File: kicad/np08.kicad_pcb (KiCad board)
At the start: 2 copper layers, 101.6 x 101.6 mm, 60 parts, among them P1 USB_B, P10 CONN_01X02, P11 CONN_01X02, P12 analog, P13 GND, P14 +5V, P15 CONN_01X08, P16 CONN_01X08, P2 CONN_01X04, P3 aliment.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

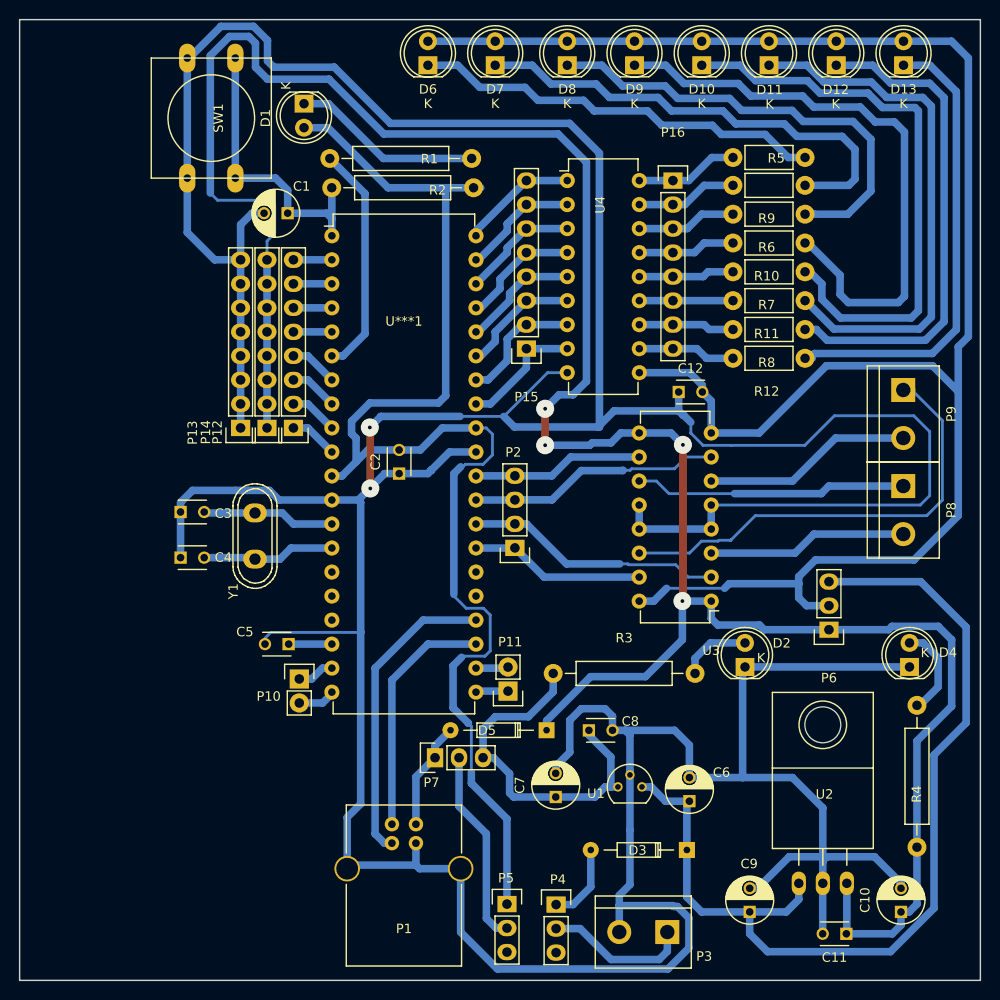
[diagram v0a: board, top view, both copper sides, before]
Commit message: prototipo base para icaro version SMD
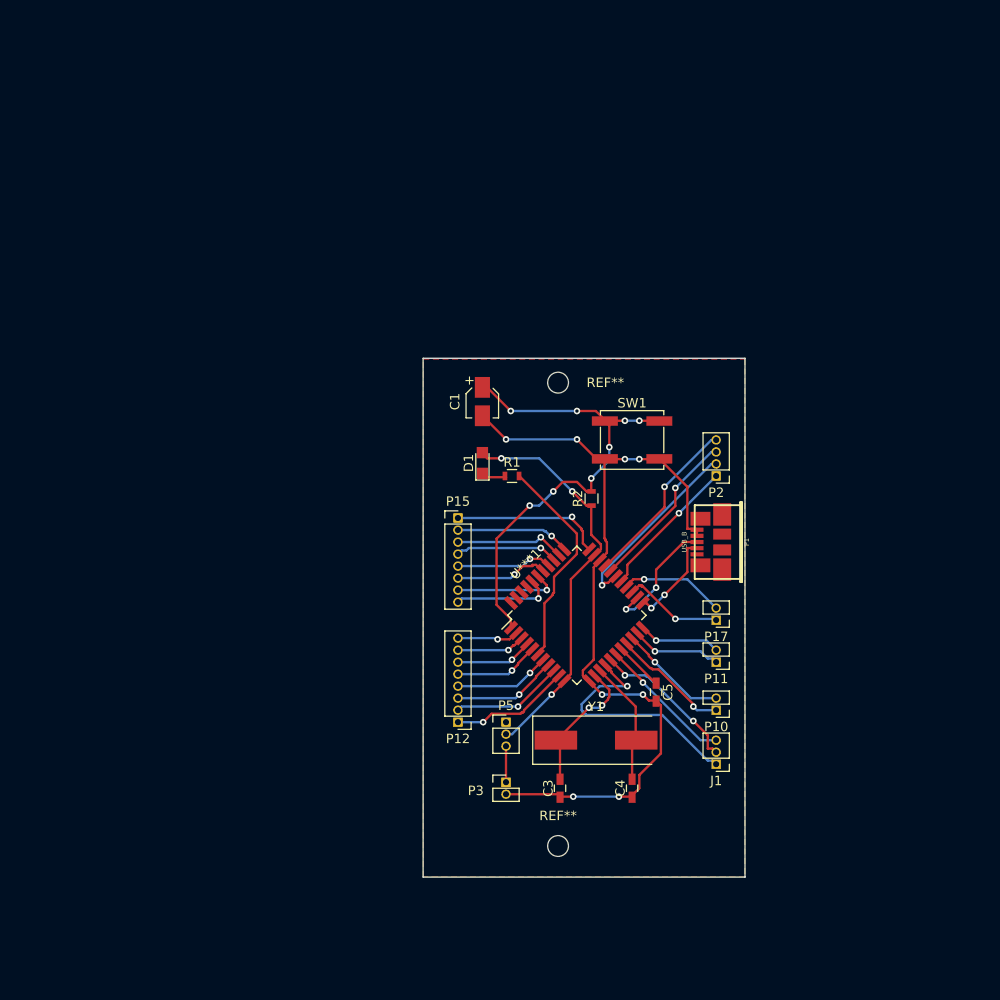
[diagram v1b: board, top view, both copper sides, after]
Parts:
- removed C10, C7: 100 uF-electr, Capacitors_ThroughHole:C_Radial_D5_L6_P2.5
- removed C11, C12, C8: 0.1uF, Capacitors_ThroughHole:C_Disc_D3_P2.5
- removed C2: C, Capacitors_ThroughHole:C_Disc_D3_P2.5
- removed C6, C9: 100uF-electr, Capacitors_ThroughHole:C_Radial_D5_L6_P2.5
- removed D10, D11, D12, D13, D2, D4, D6, D7, D8, D9: LED, LEDs:LED-5MM
- removed D3, D5: D, Diodes_ThroughHole:Diode_DO-35_SOD27_Horizontal_RM10
- removed P13: GND, Pin_Headers:Pin_Header_Straight_1x08
- removed P14: +5V, Pin_Headers:Pin_Header_Straight_1x08
- removed P16: CONN_01X08, Pin_Headers:Pin_Header_Straight_1x08
- removed P4: sw_aliment, Pin_Headers:Pin_Header_Straight_1x03
- removed P6, P7: CONN_01X03, Pin_Headers:Pin_Header_Straight_1x03
- removed P8, P9: CONN_01X02, Connect:bornier2
- removed R10, R11, R12, R5, R6, R7, R8, R9: R, Resistors_ThroughHole:Resistor_Horizontal_RM7mm
- removed R3, R4: 470, Resistors_ThroughHole:Resistor_Horizontal_RM15mm
- removed U1: LM78L05ACZ, TO_SOT_Packages_THT:TO-92_Molded_Narrow
- removed U2: LM7805CT, TO_SOT_Packages_THT:TO-220_Neutral123_Horizontal
- removed U3: L293D, Housings_DIP:DIP-16_W7.62mm
- removed U4: ULN2803, Housings_DIP:DIP-18_W7.62mm
- added J1: RC0-RC1-RC2, Pin_Headers:Pin_Header_Straight_1x03_Pitch1.27mm, F.Cu at (172.7, 133.3)
- added P17: RX-TX, Pin_Headers:Pin_Header_Straight_1x02_Pitch1.27mm, F.Cu at (172.7, 118.1)
- added REF**: , Mounting_Holes:MountingHole_2.2mm_M2, F.Cu at (156.0, 93.0)
- added REF**: , Mounting_Holes:MountingHole_2.2mm_M2, F.Cu at (156.0, 142.0)
- C1: footprint Capacitors_ThroughHole:C_Radial_D5_L6_P2.5 -> Capacitors_SMD:CP_Elec_3x5.3
- C3, C4, C5: footprint Capacitors_ThroughHole:C_Disc_D3_P2.5 -> Capacitors_SMD:C_0603_HandSoldering
- D1: footprint LEDs:LED-5MM -> LEDs:LED_0805
- P1: footprint Connect:USB_B -> w_conn_pc:conn_usb_B_micro_smd
- P10, P11: footprint Pin_Headers:Pin_Header_Straight_1x02 -> Pin_Headers:Pin_Header_Straight_1x02_Pitch1.27mm
- P12: footprint Pin_Headers:Pin_Header_Straight_1x08 -> Pin_Headers:Pin_Header_Straight_1x08_Pitch1.27mm
- P15: value CONN_01X08 -> PORTB; footprint Pin_Headers:Pin_Header_Straight_1x08 -> Pin_Headers:Pin_Header_Straight_1x08_Pitch1.27mm
- P2: footprint Pin_Headers:Pin_Header_Straight_1x04 -> Pin_Headers:Pin_Header_Straight_1x04_Pitch1.27mm
- P3: footprint Connect:bornier2 -> Pin_Headers:Pin_Header_Straight_1x02_Pitch1.27mm
- P5: footprint Pin_Headers:Pin_Header_Straight_1x03 -> Pin_Headers:Pin_Header_Straight_1x03_Pitch1.27mm
- R1, R2: footprint Resistors_ThroughHole:Resistor_Horizontal_RM15mm -> Resistors_SMD:R_0603
- SW1: footprint Buttons_Switches_ThroughHole:SW_PUSH-12mm -> Buttons_Switches_SMD:SW_SPST_EVQP0
- U***1: footprint Housings_DIP:DIP-40_W15.24mm -> Housings_QFP:LQFP-44_10x10mm_Pitch0.8mm
- Y1: footprint Crystals:Crystal_HC50-U_Vertical -> Crystals:Crystal_SMD_HC49-SD
- moved SW1 56.0 mm to (163.8, 99.1), turned to 0 degrees
- moved C4 53.6 mm to (163.8, 135.9), turned to 90 degrees
- moved C3 49.6 mm to (156.2, 135.9), turned to 90 degrees
- moved U***1 47.8 mm to (158.0, 117.6), turned to 45 degrees
- moved P10 44.2 mm to (172.7, 127.6), turned to 180 degrees
- moved P1 44.0 mm to (173.4, 109.9), turned to 90 degrees
- moved D1 42.4 mm to (148.0, 101.5), turned to 90 degrees
- moved Y1 42.0 mm to (160.0, 130.8), turned to 0 degrees
- moved C5 39.2 mm to (166.4, 125.7), turned to 270 degrees
- moved P12 35.6 mm to (145.4, 128.9)
- moved R2 35.1 mm to (159.5, 105.3), turned to 90 degrees
- moved R1 33.8 mm to (151.1, 102.9), turned to 0 degrees
- moved C1 28.6 mm to (148.0, 95.0), turned to 270 degrees
- moved P2 22.6 mm to (172.7, 102.9)
- moved P11 22.2 mm to (172.7, 122.6)
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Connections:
- P1 pad 1: VCC -> (no net)
- P3 pad 1: Net-(P3-Pad1) -> /alimentacion/uno_estos_dos_para_la_prueba_SMD
- P5 pad 1: VDD -> (no net)
- P5 pad 2: vcc_con -> VDD
- P5 pad 3: (no net) -> /alimentacion/uno_estos_dos_para_la_prueba_SMD
- U***1 pad 15: (no net) -> RC0
- U***1 pad 16: (no net) -> RC1
- U***1 pad 17: (no net) -> RC2
- U***1 pad 25: (no net) -> RC6
- U***1 pad 26: (no net) -> RC7
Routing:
- net GND: track 543.2 -> 90.0 mm, vias 2 -> 8
- net /alimentacion/5v_lm7805: track 257.1 -> 0.00 mm, vias 4 -> 0
- net /UNL2803/+5/12V: track 192.5 -> 0.00 mm
- net 12V: track 102.8 -> 0.00 mm
- net VDD: track 138.9 -> 43.3 mm, vias 0 -> 3
- net Net-(D9-Pad1): track 63.4 -> 0.00 mm
- net Net-(D10-Pad1): track 61.3 -> 0.00 mm
- net Net-(D11-Pad1): track 56.4 -> 0.00 mm
- net Net-(D12-Pad1): track 52.5 -> 0.00 mm
- net Net-(D7-Pad1): track 50.4 -> 0.00 mm
- net Net-(D13-Pad1): track 49.9 -> 0.00 mm
- net Net-(D8-Pad1): track 49.8 -> 0.00 mm
- net Net-(P9-Pad1): track 48.3 -> 0.00 mm
- net Net-(D6-Pad1): track 43.9 -> 0.00 mm
- net /alimentacion/5v_78l05: track 38.6 -> 0.00 mm
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- added copper zone on F.Cu, net GND
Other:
- board size 101.6 x 101.6 mm -> 34 x 54.9 mm
- net class Default: trace_width 0.8 -> 0.25; via_dia 1.91 -> 0.7
- rule trace_min: 0.2 -> 0.1
